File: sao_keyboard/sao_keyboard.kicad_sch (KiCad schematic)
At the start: 3 parts

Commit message: Keyboard addon Rev. 1
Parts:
- added C1, C14, C2, C3, C4, C5, C6: 100n, Capacitor_SMD:C_0402_1005Metric_Pad0.74x0.62mm_HandSolder, symbol Device:C_Small
- added H1: MountingHole_Pad, MountingHole:MountingHole_2.2mm_M2_Pad_Via, symbol Mechanical:MountingHole_Pad
- added J4, J5: I2C, qwiic:1X04_1MM_RA_GND, symbol qwiic:qwiic
- added J6: sao_v2_addon_tht, simple_add_on_v2:sao_v2_addon_tht, symbol simple_add_on_v2:sao_v2_addon_tht
- added R1, R10, R11, R12, R13, R14, R15, R16, R17, R18, R19, R2, R20, R21, R22, R23, R24, R25, R26, R27, R28, R29, R3, R30, R31, R32, R33, R34, R35, R36, R4, R5, R6, R7, R8, R9: 1K, Resistor_SMD:R_0402_1005Metric_Pad0.72x0.64mm_HandSolder, symbol Device:R
- added U1, U2, U3, U4, U5: 74LS245, Package_SO:TSSOP-20_4.4x6.5mm_P0.65mm, symbol 74xx:74LS245
- added U3: 24LC00, Package_SO:SOIC-8_3.9x4.9mm_P1.27mm, symbol Memory_EEPROM:24LC00
- added U6: CH32V003F4P6, Package_SO:TSSOP-20_4.4x6.5mm_P0.65mm, symbol ch32v003:CH32V003F4P6
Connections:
- net X0Y0: now reaches J1.1 (C)
- net X0Y0: now also R1.2, U1.9 (A7)
- net X1Y1: now reaches J1.10 (A)
- net X1Y1: now also R10.2, U2.8 (A6)
- net X1Y2: now reaches J1.11 (A#)
- net X1Y2: now also R11.2, U2.7 (A5)
- net X1Y3: now reaches J1.12 (B)
- net X1Y3: now also R12.2, U2.6 (A4)
- net X0Y1: now reaches J1.2 (C#)
- net X0Y1: now also R2.2, U1.8 (A6)
- net X0Y2: now reaches J1.3 (D)
- net X0Y2: now also R3.2, U1.7 (A5)
- net X0Y3: now reaches J1.4 (D#)
- net X0Y3: now also R4.2, U1.6 (A4)
- net X0Y4: now reaches J1.5 (E)
- net X0Y4: now also R5.2, U1.5 (A3)
- net X0Y5: now reaches J1.6 (F)
- net X0Y5: now also R6.2, U1.4 (A2)
- net X0Y6: now reaches J1.7 (F#)
- net X0Y6: now also R7.2, U1.3 (A1)
- net X0Y7: now reaches J1.8 (G)
- net X0Y7: now also R8.2, U1.2 (A0)
- net X1Y0: now reaches J1.9 (G#)
- net X1Y0: now also R9.2, U2.9 (A7)
- net X1Y4: now reaches J2.1 (C)
- net X1Y4: now also R13.2, U2.5 (A3)
- net X2Y5: now reaches J2.10 (A)
- net X2Y5: now also R22.2, U3.4 (A2)
- net X2Y6: now reaches J2.11 (A#)
- net X2Y6: now also R23.2, U3.3 (A1)
- net X2Y7: now reaches J2.12 (B)
- net X2Y7: now also R24.2, U3.2 (A0)
- net X1Y5: now reaches J2.2 (C#)
- net X1Y5: now also R14.2, U2.4 (A2)
- net X1Y6: now reaches J2.3 (D)
- net X1Y6: now also R15.2, U2.3 (A1)
- net X1Y7: now reaches J2.4 (D#)
- net X1Y7: now also R16.2, U2.2 (A0)
- net X2Y0: now reaches J2.5 (E)
- net X2Y0: now also R17.2, U3.9 (A7)
- net X2Y1: now reaches J2.6 (F)
- net X2Y1: now also R18.2, U3.8 (A6)
- net X2Y2: now reaches J2.7 (F#)
- net X2Y2: now also R19.2, U3.7 (A5)
- net X2Y3: now reaches J2.8 (G)
- net X2Y3: now also R20.2, U3.6 (A4)
- net X2Y4: now reaches J2.9 (G#)
- net X2Y4: now also R21.2, U3.5 (A3)
- net X3Y0: now reaches J3.1 (C)
- net X3Y0: now also R25.2, U4.9 (A7)
- net X4Y1: now reaches J3.10 (A)
- net X4Y1: now also R34.2, U5.8 (A6)
- net X4Y2: now reaches J3.11 (A#)
- net X4Y2: now also R35.2, U5.7 (A5)
- net X4Y3: now reaches J3.12 (B)
- net X4Y3: now also R36.2, U5.6 (A4)
- net X3Y1: now reaches J3.2 (C#)
- net X3Y1: now also R26.2, U4.8 (A6)
- net X3Y2: now reaches J3.3 (D)
- net X3Y2: now also R27.2, U4.7 (A5)
- net X3Y3: now reaches J3.4 (D#)
- net X3Y3: now also R28.2, U4.6 (A4)
- net X3Y4: now reaches J3.5 (E)
- net X3Y4: now also R29.2, U4.5 (A3)
- net X3Y5: now reaches J3.6 (F)
- net X3Y5: now also R30.2, U4.4 (A2)
- net X3Y6: now reaches J3.7 (F#)
- net X3Y6: now also R31.2, U4.3 (A1)
- net X3Y7: now reaches J3.8 (G)
- net X3Y7: now also R32.2, U4.2 (A0)
- net X4Y0: now reaches J3.9 (G#)
- net X4Y0: now also R33.2, U5.9 (A7)
- new net +3V3: C1.1, C14.1, C2.1, C3.1, C4.1, C5.1, C6.1, J4.2 (VCC), J5.2 (VCC), J6.1 (3V3), R1.1, R10.1, R11.1, R12.1, R13.1, R14.1, R15.1, R16.1, R17.1, R18.1, R19.1, R2.1, R20.1, R21.1, R22.1, R23.1, R24.1, R25.1, R26.1, R27.1, R28.1, R29.1, R3.1, R30.1, R31.1, R32.1, R33.1, R34.1, R35.1, R36.1, R4.1, R5.1, R6.1, R7.1, R8.1, R9.1, U1.1 (A->B), U1.20 (VCC), U2.1 (A->B), U2.20 (VCC), U3.1 (A->B), U3.20 (VCC), U3.8 (VCC), U4.1 (A->B), U4.20 (VCC), U5.1 (A->B), U5.20 (VCC), U6.7 (VSS)
- new net GND: C1.2, C14.2, C2.2, C3.2, C4.2, C5.2, C6.2, H1.1, J4.1 (GND), J4.5, J4.6, J5.1 (GND), J5.5, J5.6, J6.2 (GND), U1.10 (GND), U2.10 (GND), U3.1 (A0), U3.10 (GND), U3.2 (A1), U3.3 (A2), U3.4 (GND), U3.7 (WP), U4.10 (GND), U5.10 (GND), U5.2 (A0), U5.3 (A1), U5.4 (A2), U5.5 (A3), U6.9 (VDD)
- new net SCL: J4.4 (SCL), J5.4 (SCL), J6.4 (SCL), U3.6 (SCL), U6.15 (PC5)
- new net SDA: J4.3 (SDA), J5.3 (SDA), J6.3 (SDA), U3.5 (SDA), U6.16 (PC6)
- new net X0: U1.19 (CE), U6.8 (PD0)
- new net X1: U2.19 (CE), U6.18 (PD1)
- new net X2: U3.19 (CE), U6.19 (PD2)
- new net X3: U4.19 (CE), U6.20 (PD3)
- new net X4: U5.19 (CE), U6.1 (PD4)
- new net Y0: U1.11 (B7), U2.11 (B7), U3.11 (B7), U4.11 (B7), U5.11 (B7), U6.17 (PC7)
- new net Y1: U1.12 (B6), U2.12 (B6), U3.12 (B6), U4.12 (B6), U5.12 (B6), U6.3 (PD6)
- new net Y2: U1.13 (B5), U2.13 (B5), U3.13 (B5), U4.13 (B5), U5.13 (B5), U6.2 (PD5)
- new net Y3: U1.14 (B4), U2.14 (B4), U3.14 (B4), U4.14 (B4), U5.14 (B4), U6.14 (PC4)
- new net Y4: U1.15 (B3), U2.15 (B3), U3.15 (B3), U4.15 (B3), U5.15 (B3), U6.13 (PC3)
- new net Y5: U1.16 (B2), U2.16 (B2), U3.16 (B2), U4.16 (B2), U5.16 (B2), U6.12 (PC2)
- new net Y6: U1.17 (B1), U2.17 (B1), U3.17 (B1), U4.17 (B1), U5.17 (B1), U6.11 (PC1)
- new net Y7: U1.18 (B0), U2.18 (B0), U3.18 (B0), U4.18 (B0), U5.18 (B0), U6.10 (PC0)
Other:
- moved on the sheet: J1, J2, J3

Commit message: Curvify the keyboard
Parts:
- H1: now left out of the parts list
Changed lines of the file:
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@@
   )
   (symbol (lib_id "Mechanical:MountingHole_Pad") (at 40.64 68.58 90) (unit 1)
-    (in_bom yes) (on_board yes) (dnp no)
+    (in_bom no) (on_board yes) (dnp no)
     (property "Reference" "H1" (at 36.83 67.31 90) (do_not_autoplace)
       (effects (font (size 1.27 1.27)) (justify left))

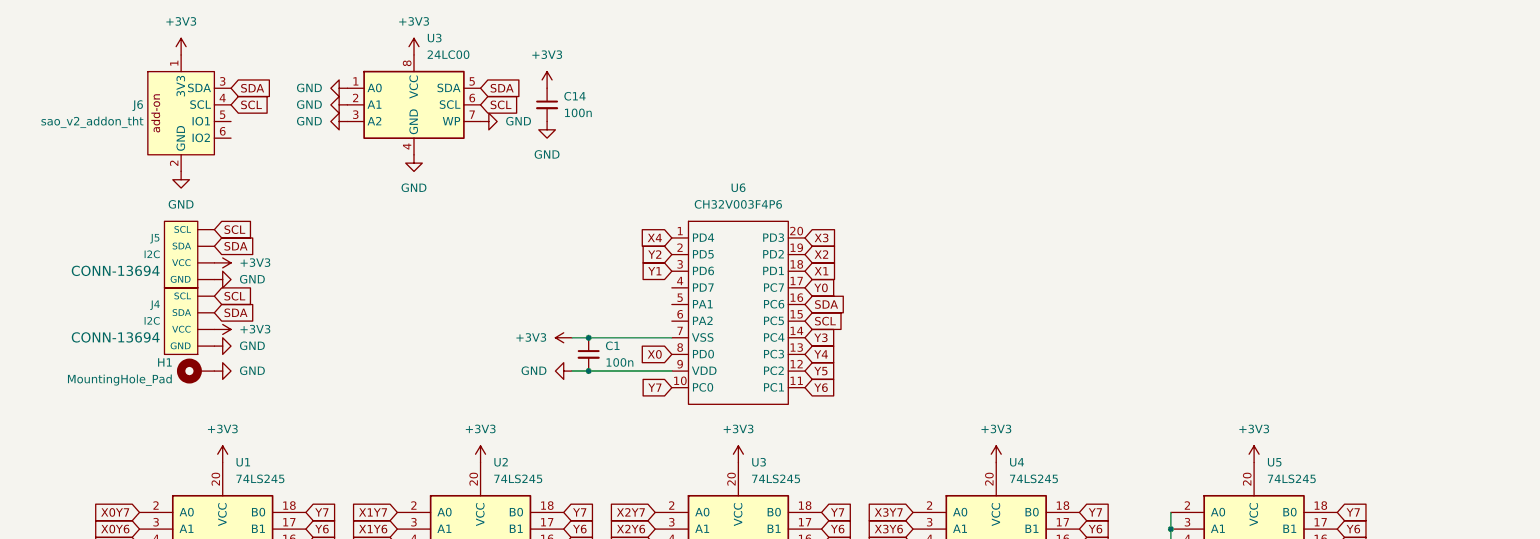
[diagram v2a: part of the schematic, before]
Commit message: Add some lights to the keyboard addon.
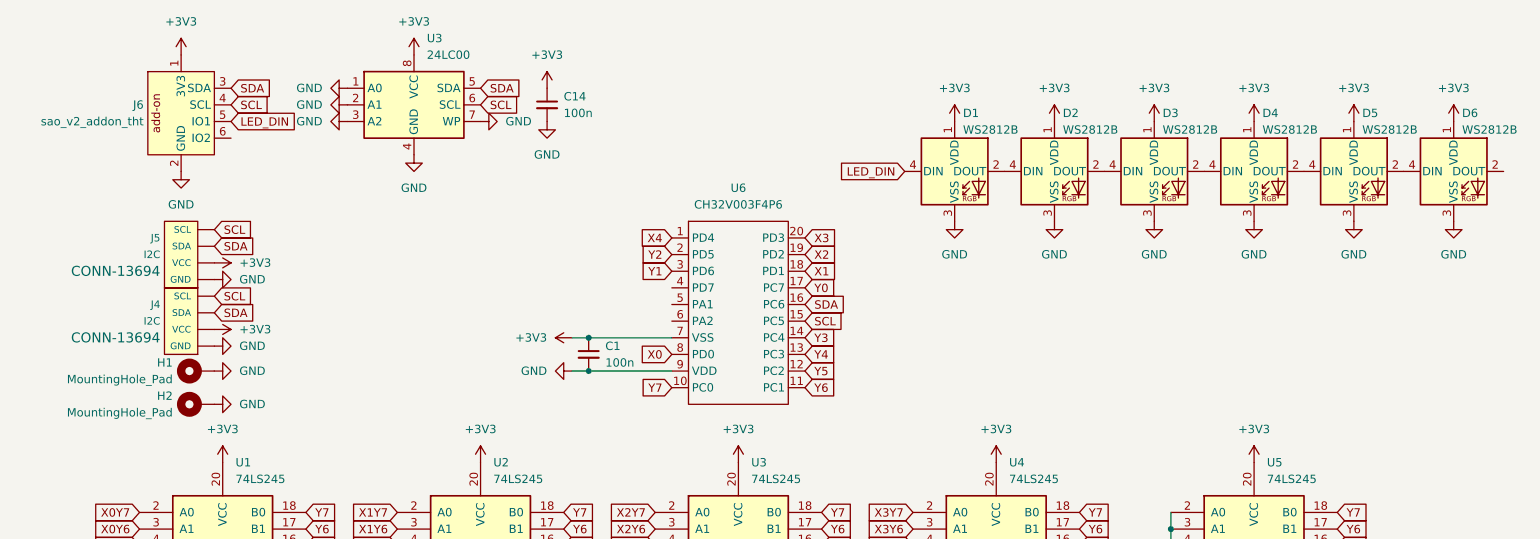
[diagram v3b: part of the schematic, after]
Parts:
- added D1, D2, D3, D4, D5, D6: WS2812B, LED_SMD:LED_WS2812B_PLCC4_5.0x5.0mm_P3.2mm, symbol LED:WS2812B
- added H2: MountingHole_Pad, MountingHole:MountingHole_2.2mm_M2_Pad_Via, symbol Mechanical:MountingHole_Pad
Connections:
- net +3V3: now also D1.1 (VDD), D2.1 (VDD), D3.1 (VDD), D4.1 (VDD), D5.1 (VDD), D6.1 (VDD)
- net GND: now also D1.3 (VSS), D2.3 (VSS), D3.3 (VSS), D4.3 (VSS), D5.3 (VSS), D6.3 (VSS), H2.1
- net LED_DIN: now reaches J6.5 (IO1)
- net LED_DIN: now also D1.4 (DIN)
- new net: D5.2 (DOUT), D6.4 (DIN)
- new net: D4.2 (DOUT), D5.4 (DIN)
- new net: D1.2 (DOUT), D2.4 (DIN)
- new net: D3.2 (DOUT), D4.4 (DIN)
- new net: D2.2 (DOUT), D3.4 (DIN)

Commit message: Finish the keyboard design
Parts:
- added R37: 1K, Resistor_SMD:R_0402_1005Metric_Pad0.72x0.64mm_HandSolder, symbol Device:R
- D1, D2, D3, D4, D5, D6: footprint LED_SMD:LED_WS2812B_PLCC4_5.0x5.0mm_P3.2mm -> not_ugly_ws2812b:LED_WS2812B_PLCC4_5.0x5.0mm_P3.2mm
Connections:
- net +3V3: now also R37.1
- net X1: now also U6.4 (PD7); no longer U6.18 (PD1)
- net SWIO: now reaches J6.6 (IO2)
- net SWIO: now also U6.18 (PD1), R37.2
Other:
- moved on the sheet: D1, D2, D3, D4, D5, D6
